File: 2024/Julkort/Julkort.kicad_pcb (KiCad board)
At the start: 2 copper layers, 98.8 x 68 mm, 29 parts, among them J1 SK-3296S-01-L1, U1 ATtiny44A-M, U2 L78L05_SOT89

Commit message: 2024 v1
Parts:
- removed G***: LOGO, gra:wwwwwwwwwwwwwwwwww
- removed J1: SK-3296S-01-L1, ProLib_pcs_2024-11-12:SW-SMD_3P-P1.50_L2.7-W6.6
- removed U2: L78L05_SOT89, Package_TO_SOT_SMD:SOT-89-3
- USBC1: moved to F.Cu
- moved D1 70.4 mm to (117.5, 127.2)
- moved S1 63.6 mm to (138.5, 145.2)
- moved D5 61.2 mm to (144.2, 111.3)
- moved D6 57.3 mm to (129.7, 104.2)
- moved USBC1 56.5 mm to (119.7, 145.1), turned to -90 degrees
- moved D2 53.9 mm to (124.0, 122.5)
- moved TP5 51.7 mm to (118.6, 143.7)
- moved TP6 51.7 mm to (118.7, 146.8)
- moved D4 45.7 mm to (135.7, 120.0)
- moved D3 44.4 mm to (142.2, 124.5), turned to 90 degrees
- moved D16 40.7 mm to (130.4, 64.7), turned to 180 degrees
- moved U1 40.1 mm to (129.4, 145.1)
- moved R1 39.4 mm to (129.7, 138.2), turned to 90 degrees
- moved TP1 37.7 mm to (133.5, 142.5)
- moved TP2 37.7 mm to (136.1, 142.5)
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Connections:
- USBC1 pad 0: Net-(J1-COM) -> GND
- USBC1 pad 1: Net-(J1-COM) -> GND
- USBC1 pad 2: Net-(J1-COM) -> GND
- USBC1 pad 3: Net-(J1-COM) -> GND
- USBC1 pad A1: Net-(J1-COM) -> GND
- USBC1 pad A12: Net-(J1-COM) -> GND
- USBC1 pad A4: Net-(U2-IN) -> VCC_REG
- USBC1 pad A9: Net-(U2-IN) -> VCC_REG
- USBC1 pad B1: Net-(J1-COM) -> GND
- USBC1 pad B12: Net-(J1-COM) -> GND
- USBC1 pad B4: Net-(U2-IN) -> VCC_REG
- USBC1 pad B9: Net-(U2-IN) -> VCC_REG
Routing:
- net VCC_REG: track 310.5 -> 23.8 mm, vias 19 -> 15
- net Net-(U2-IN): track 96.3 -> 0.00 mm, vias 1 -> 0
- net Net-(U1-PA1): track 85.5 -> 24.6 mm
- net Net-(J1-COM): track 42.9 -> 0.00 mm, vias 1 -> 0
- net Net-(D1-DIN): track 42.7 -> 18.0 mm, vias 0 -> 2
- net GND: track 41.0 -> 17.8 mm, vias 20 -> 3
- net Net-(D4-DOUT): track 25.4 -> 11.6 mm, vias 0 -> 2
- net Net-(D1-DOUT): track 18.4 -> 7.17 mm
- net Net-(D3-DOUT): track 18.9 -> 7.99 mm
- net Net-(D10-DIN): track 14.4 -> 6.51 mm
- net Net-(U1-AREF/PA0): track 18.6 -> 11.1 mm
- net Net-(D14-DOUT): track 8.53 -> 1.10 mm
- net Net-(D8-DOUT): track 15.0 -> 8.19 mm
- net Net-(D15-DOUT): track 7.84 -> 1.10 mm
- net Net-(D6-DOUT): track 22.6 -> 16.0 mm
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- added copper zone on F.Cu, net GND
- added copper zone on B.Cu, net VCC_REG
- removed copper zone on B.Cu, net GND
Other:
- board size 98.8 x 68 mm -> 49.1 x 95.9 mm
- board text removed: "C.A.S.E 23/24"
- board text removed: "God jul önskar"

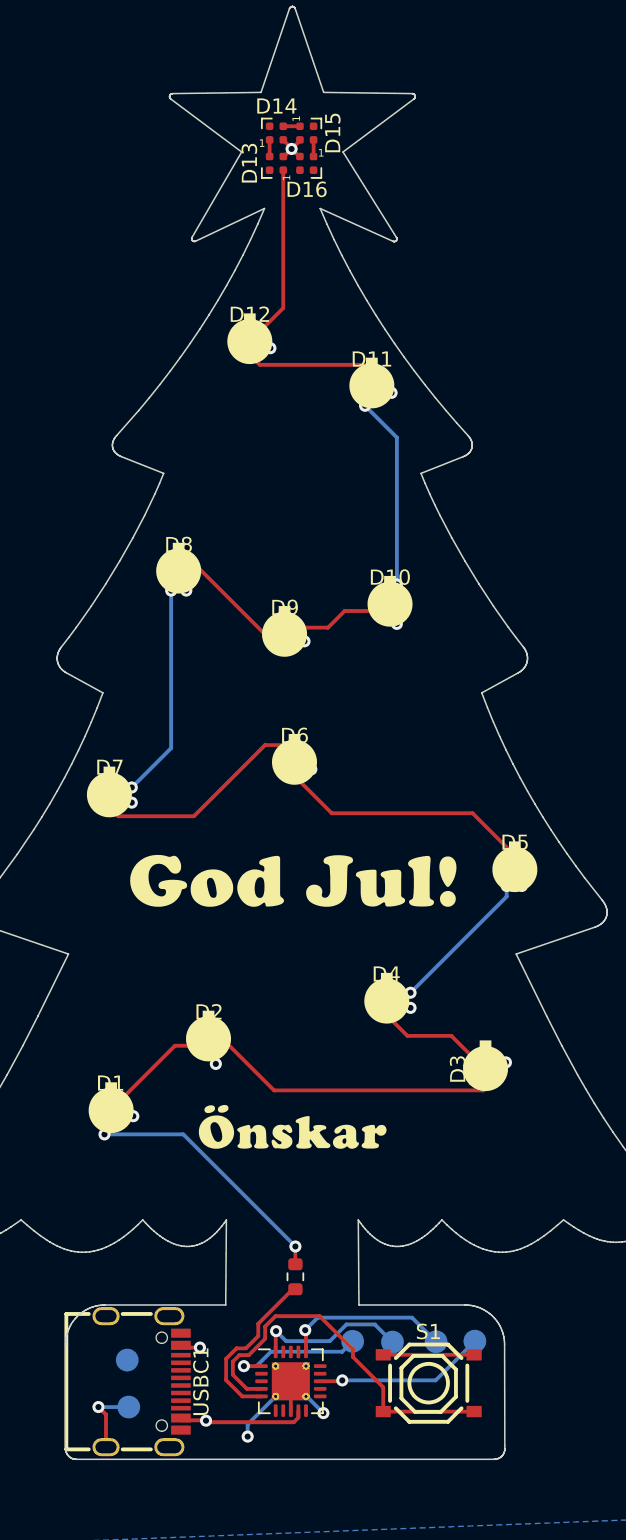
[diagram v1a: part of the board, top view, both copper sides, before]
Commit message: Byte av atmega44-footprint
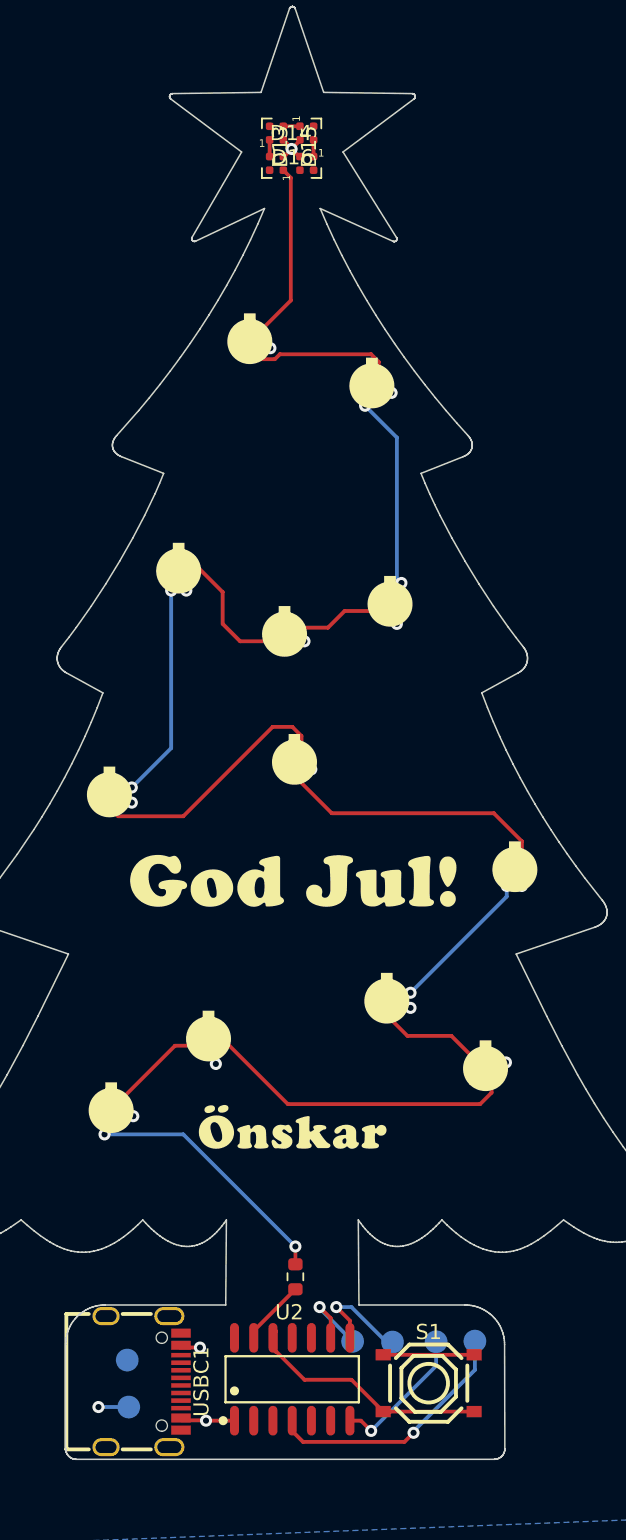
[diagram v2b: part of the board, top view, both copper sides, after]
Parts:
- removed U1: ATtiny44A-M, Package_DFN_QFN:QFN-20-1EP_4x4mm_P0.5mm_EP2.5x2.5mm_ThermalVias
- added U2: ~, footprint:SOP-14_L8.6-W3.9-P1.27-LS6.0-BL, F.Cu at (129.5, 145.0)
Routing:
- net GND: track 17.8 -> 8.00 mm, vias 3 -> 1
- net Net-(U2-PA1(ADC1/AIN0/PCINT1)): track 24.6 -> 17.1 mm
- net Net-(U2-PA0(ADC0/AREF/PCINT0)): track 11.1 -> 4.35 mm
- net Net-(U2-PB3_(PCINT11/RESET#/dW)): track 11.3 -> 17.0 mm
- net VCC_REG: track 23.8 -> 18.9 mm
- net Net-(U2-PA4(ADC4/USCK/SCL/T1/PCINT4)): track 9.02 -> 5.50 mm
- net Net-(U2-PA5(ADC5/DO/MISO/OC1B/PCINT5)): track 10.3 -> 7.07 mm
- net Net-(U2-PA6(PCINT6/OC1A/SDA/MOSI/DI/ADC6)): track 11.1 -> 9.34 mm
- net Net-(D6-DOUT): track 16.0 -> 17.5 mm
- net Net-(D8-DOUT): track 8.19 -> 9.42 mm
- net Net-(D2-DOUT): track 20.4 -> 21.6 mm
- net Net-(D11-DOUT): track 9.80 -> 10.7 mm
- net Net-(D5-DOUT): track 18.0 -> 18.8 mm
